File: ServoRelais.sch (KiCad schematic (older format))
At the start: 14 parts, among them J1 Conn_01x03_Female, J2 ISCP, J3 Conn_01x02_Female, J4 Conn_01x03_Female, U1 L78L05_SOT89, U2 PIC10F320-IP, U3 ASSR-1611

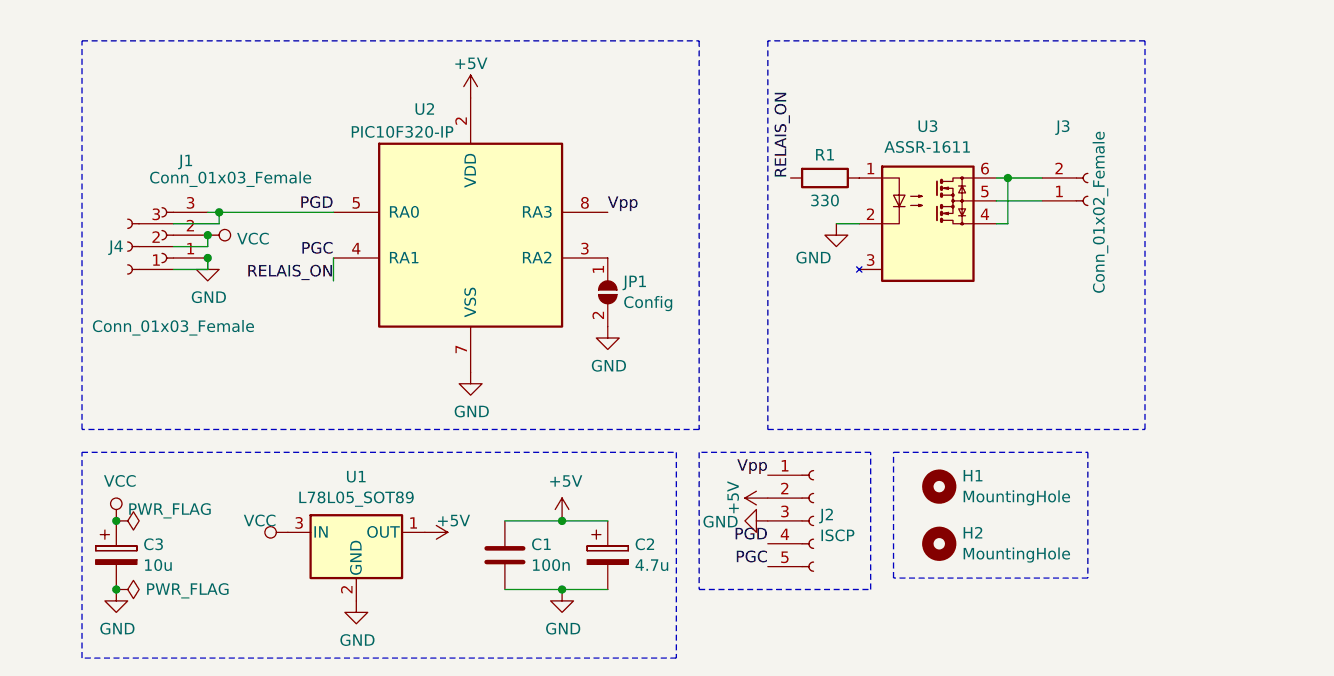
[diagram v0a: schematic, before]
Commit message: finish PCB, using ASSR-1611 as a 5A circuit breaker.
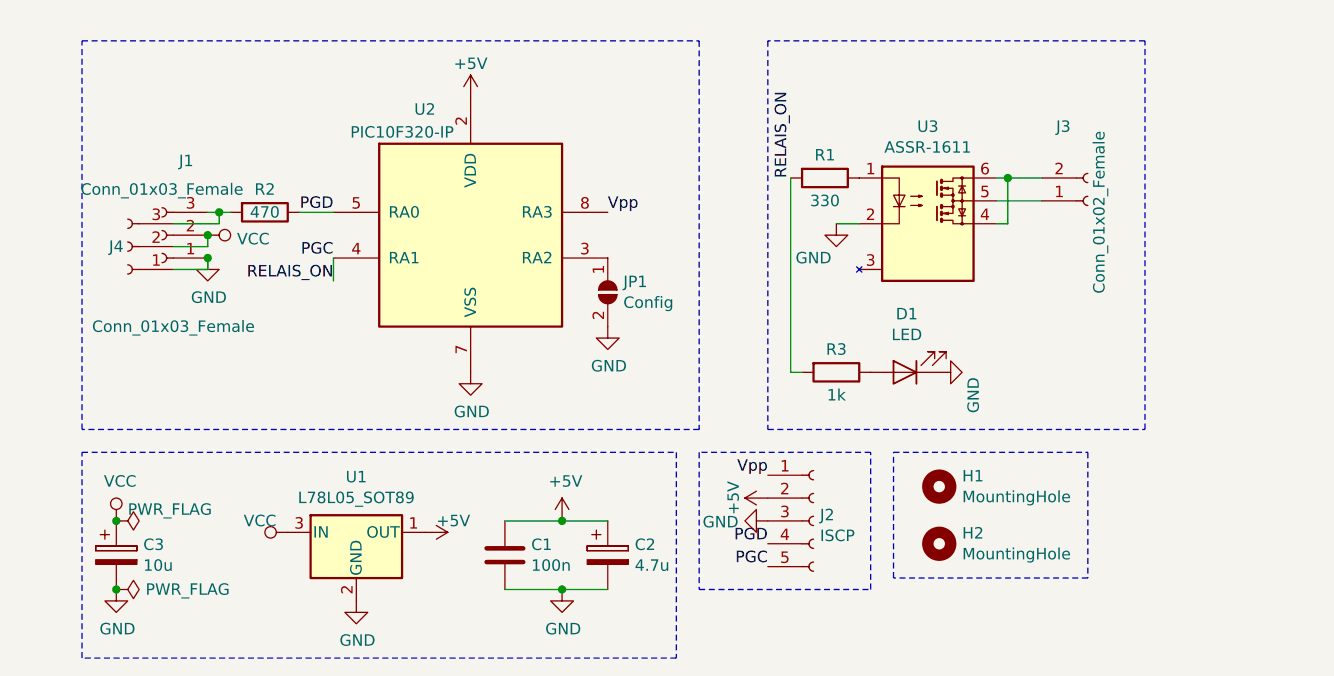
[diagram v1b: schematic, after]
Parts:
- added D1: LED, LEDs:LED_D3.0mm, symbol Device:LED
- added R2: 470, Resistors_ThroughHole:R_Axial_DIN0207_L6.3mm_D2.5mm_P7.62mm_Horizontal, symbol Device:R
- added R3: 1k, Resistors_ThroughHole:R_Axial_DIN0207_L6.3mm_D2.5mm_P7.62mm_Horizontal, symbol Device:R
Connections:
- net GND: now also D1.1 (K)
- net PGC: now also R3.2
- net PGD: now also R2.1; no longer J1.3 (Pin_3), J4.3 (Pin_3)
- new net: J1.3 (Pin_3), J4.3 (Pin_3), R2.2
- new net: D1.2 (A), R3.1
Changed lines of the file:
@@
 P 1050 1450
 F 0 "J1" H 944 1125 50  0000 C CNN
-F 1 "Conn_01x03_Female" H 750 1200 50  0000 C CNN
+F 1 "Conn_01x03_Female" H 1050 1250 50  0000 C CNN
 F 2 "Connectors_Molex:Molex_KK-6410-03_03x2.54mm_Straight" H 1050 1450 50  0001 C CNN
 F 3 "~" H 1050 1450 50  0001 C CNN
@@
 Wire Wire Line
 	1300 1400 1300 1350
-Connection ~ 1300 1350
-Wire Wire Line
-	1300 1350 1800 1350
 Wire Wire Line
 	1100 1500 1250 1500
@@
 $EndComp
 Connection ~ 850  2700
+$Comp
+L Device:R R2
+U 1 1 5FAE5A28
+P 1500 1350
+F 0 "R2" V 1400 1350 50  0000 C CNN
+F 1 "470" V 1500 1350 50  0000 C CNN
+F 2 "Resistors_ThroughHole:R_Axial_DIN0207_L6.3mm_D2.5mm_P7.62mm_Horizontal" V 1430 1350 50  0001 C CNN
+F 3 "~" H 1500 1350 50  0001 C CNN
+	1    1500 1350
+	0    1    1    0
+$EndComp
+Wire Wire Line
+	1300 1350 1350 1350
+Connection ~ 1300 1350
+Wire Wire Line
+	1650 1350 1800 1350
+$Comp
+L Device:R R3
+U 1 1 5FAE63BB
+P 4000 2050
+F 0 "R3" V 3900 2050 50  0000 C CNN
+F 1 "1k" V 4100 2050 50  0000 C CNN
+F 2 "Resistors_ThroughHole:R_Axial_DIN0207_L6.3mm_D2.5mm_P7.62mm_Horizontal" V 3930 2050 50  0001 C CNN
+F 3 "~" H 4000 2050 50  0001 C CNN
+	1    4000 2050
+	0    1    1    0
+$EndComp
+Wire Wire Line
+	3800 1200 3800 2050
+Wire Wire Line
+	3800 2050 3850 2050
+$Comp
+L Device:LED D1
+U 1 1 5FAE68AF
+P 4300 2050
+F 0 "D1" H 4292 1795 50  0000 C CNN
+F 1 "LED" H 4292 1886 50  0000 C CNN
+F 2 "LEDs:LED_D3.0mm" H 4300 2050 50  0001 C CNN
+F 3 "~" H 4300 2050 50  0001 C CNN
+	1    4300 2050
+	-1   0    0    1
+$EndComp
+$Comp
+L power:GND #PWR0116
+U 1 1 5FAE6927
+P 4450 2050
+F 0 "#PWR0116" H 4450 1800 50  0001 C CNN
+F 1 "GND" H 4350 1900 50  0000 C CNN
+F 2 "" H 4450 2050 50  0001 C CNN
+F 3 "" H 4450 2050 50  0001 C CNN
+	1    4450 2050
+	0    -1   -1   0
+$EndComp
 $EndSCHEMATC

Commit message: use a 3v->9V dc-dc converter. version 1.3
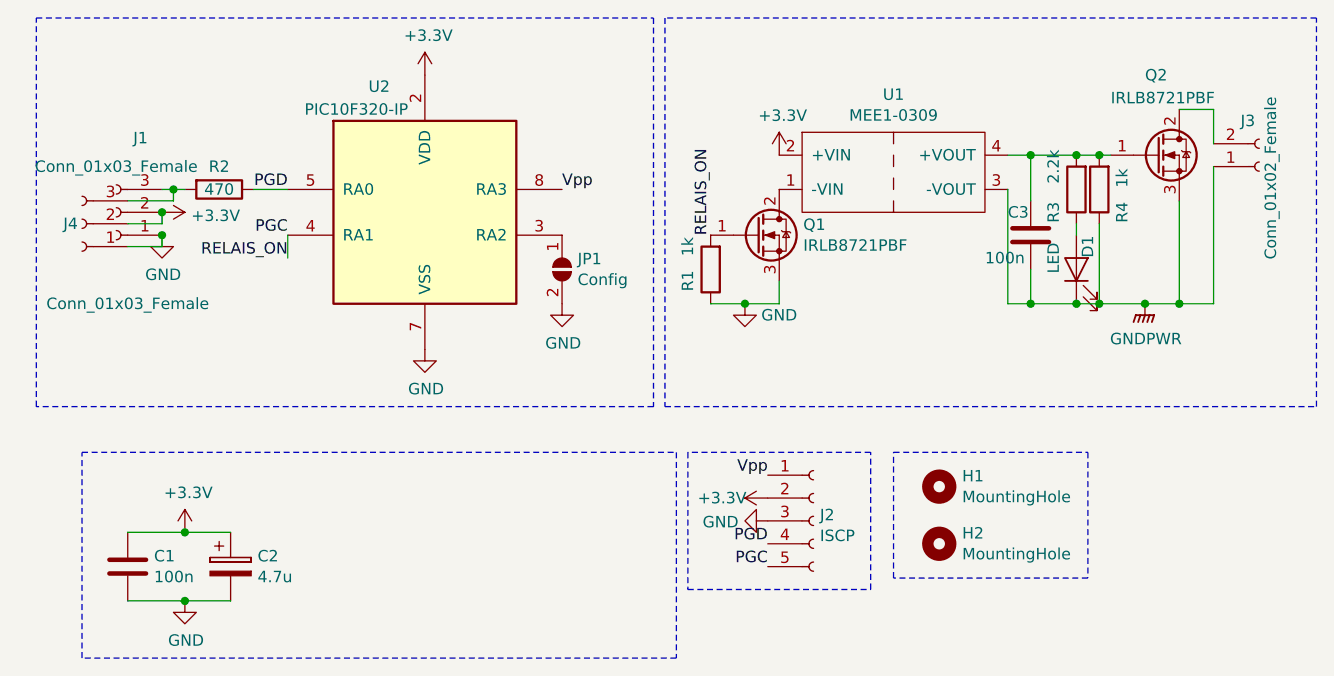
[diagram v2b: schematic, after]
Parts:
- removed C3: 10u, Capacitors_ThroughHole:CP_Radial_D4.0mm_P1.50mm, symbol Device:CP
- removed U1: L78L05_SOT89, TO_SOT_Packages_SMD:SOT-89-3_Handsoldering, symbol Regulator_Linear:L78L05_SOT89
- removed U3: ASSR-1611, Housings_DIP:DIP-6_W7.62mm_LongPads, symbol ServoRelais-rescue:ASSR-1611-ServoRelais
- added C3: 100n, Capacitors_ThroughHole:C_Rect_L4.6mm_W2.0mm_P2.50mm_MKS02_FKP02, symbol Device:C
- added Q1, Q2: IRLB8721PBF, TO_SOT_Packages_SMD:TO-252-2, symbol Transistor_FET:IRLB8721PBF
- added R4: 1k, Resistors_ThroughHole:R_Axial_DIN0207_L6.3mm_D2.5mm_P7.62mm_Horizontal, symbol Device:R
- added U1: MEE1-0309, Converters_DCDC_ACDC:DCDC-Conv_muRata_CRE1xxxxxxSC, symbol ServoRelais:MurataMEE1
- R1: value 330 -> 1k
- R3: value 1k -> 2.2k
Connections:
- net VCC is gone; now on net +3V3: J1.2 (Pin_2), J4.2 (Pin_2)
- net GND: now also R1.1, Q1.3 (S); no longer D1.1 (K)
- net PGC: now also Q1.1 (G); no longer R3.2
- net GNDPWR: now reaches J3.1 (Pin_1)
- net GNDPWR: now also D1.1 (K), C3.2, Q2.3 (S), R4.1, U1.3 (-VOUT)
- net at J3.2 (Pin_2): now also Q2.2 (D)
- net +5V renamed +3V3
- net +3V3: now also U1.2 (+VIN)
- new net: C3.1, Q2.1 (G), R3.2, R4.2, U1.4 (+VOUT)
- new net: Q1.2 (D), U1.1 (-VIN)
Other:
- moved on the sheet: C1, C2, D1, J1, J3, J4, JP1, R2, R3, U2

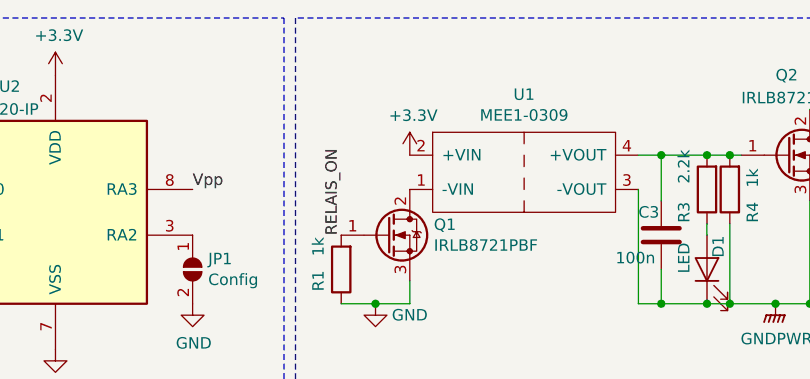
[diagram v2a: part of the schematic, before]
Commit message: PCB: add solder-switch to disable powering the DC-DC converter (else programming of the PIC fails because of power loss)
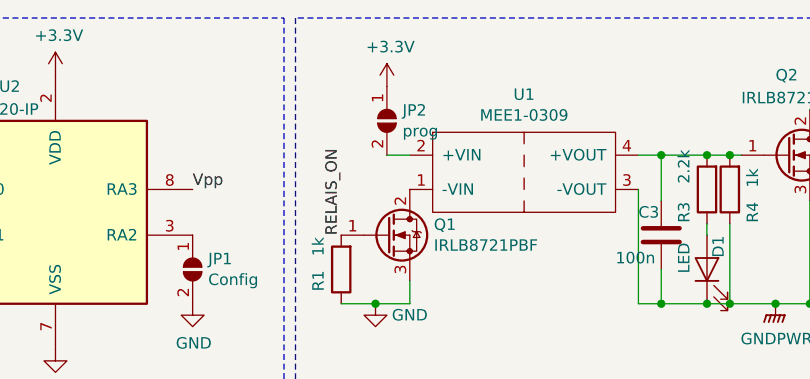
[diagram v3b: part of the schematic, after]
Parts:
- added JP2: prog, Connect:GS2, symbol Jumper:SolderJumper_2_Open
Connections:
- net +3V3: now also JP2.1 (A); no longer U1.2 (+VIN)
- new net: JP2.2 (B), U1.2 (+VIN)
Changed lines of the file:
@@
 L power:+3.3V #PWR04
 U 1 1 5FB40A3A
-P 3750 1100
-F 0 "#PWR04" H 3750 950 50  0001 C CNN
-F 1 "+3.3V" H 3765 1273 50  0000 C CNN
-F 2 "" H 3750 1100 50  0001 C CNN
-F 3 "" H 3750 1100 50  0001 C CNN
-	1    3750 1100
+P 3650 800
+F 0 "#PWR04" H 3650 650 50  0001 C CNN
+F 1 "+3.3V" H 3665 973 50  0000 C CNN
+F 2 "" H 3650 800 50  0001 C CNN
+F 3 "" H 3650 800 50  0001 C CNN
+	1    3650 800
 	1    0    0    -1
 $EndComp
@@
 Wire Wire Line
 	4850 1750 5050 1750
+$Comp
+L Jumper:SolderJumper_2_Open JP2
+U 1 1 5FB55293
+P 3650 950
+F 0 "JP2" V 3604 1018 50  0000 L CNN
+F 1 "prog" V 3695 1018 50  0000 L CNN
+F 2 "Connect:GS2" H 3650 950 50  0001 C CNN
+F 3 "~" H 3650 950 50  0001 C CNN
+	1    3650 950
+	0    1    1    0
+$EndComp
+Wire Wire Line
+	3650 1100 3750 1100
 $EndSCHEMATC

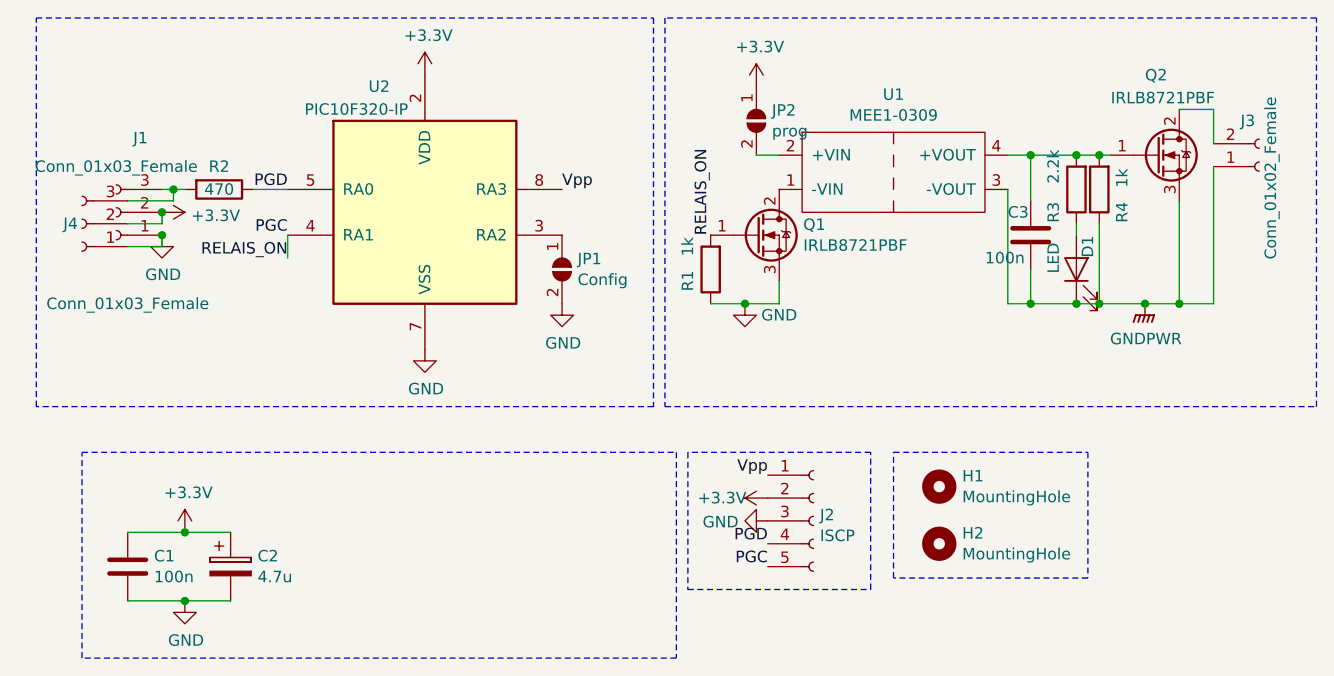
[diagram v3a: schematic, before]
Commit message: PCB 1.2: add 25Vmax->3V3 regulator
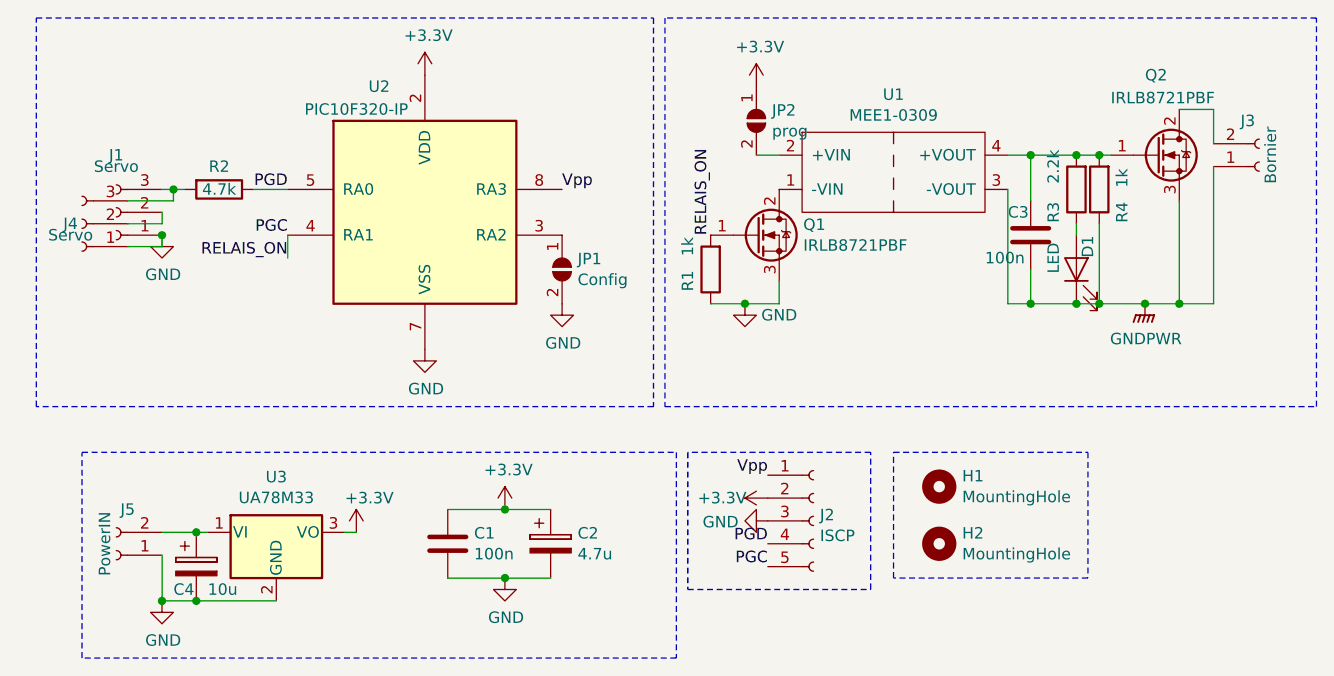
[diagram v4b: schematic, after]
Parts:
- added C4: 10u, Capacitors_ThroughHole:CP_Radial_D4.0mm_P1.50mm, symbol Device:CP
- added J5: PowerIN, Connectors_Molex:Molex_KK-6410-02_02x2.54mm_Straight, symbol Connector:Conn_01x02_Female
- added U3: UA78M33, TO_SOT_Packages_SMD:SOT-223-3_TabPin2, symbol Regulator_Linear:TC1262-33
- J1, J4: value Conn_01x03_Female -> Servo
- J3: value Conn_01x02_Female -> Bornier
- R2: value 470 -> 4.7k
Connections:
- net +3V3: now also U3.3 (VO); no longer J1.2 (Pin_2), J4.2 (Pin_2)
- net GND: now also C4.2, J5.1 (Pin_1), U3.2 (GND)
- new net: J1.2 (Pin_2), J4.2 (Pin_2)
- new net: C4.1, J5.2 (Pin_2), U3.1 (VI)
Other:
- moved on the sheet: C1, C2
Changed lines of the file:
@@
 Sheet 1 1
 Title "ServoRelais"
-Date "2020-11-12"
-Rev "1"
+Date "2020-12-22"
+Rev "1.2"
 Comp "metalu.net"
 Comment1 ""
@@
 U 1 1 5FAAD2A2
 P 850 1350
-F 0 "J1" H 744 1025 50  0000 C CNN
-F 1 "Conn_01x03_Female" H 850 1150 50  0000 C CNN
+F 0 "J1" H 850 1100 50  0000 C CNN
+F 1 "Servo" H 850 1150 50  0000 C CNN
 F 2 "Connectors_Molex:Molex_KK-6410-03_03x2.54mm_Straight" H 850 1350 50  0001 C CNN
 F 3 "~" H 850 1350 50  0001 C CNN
@@
 P 5850 1150
 F 0 "J3" H 5800 950 50  0000 C CNN
-F 1 "Conn_01x02_Female" V 5900 1200 50  0000 C CNN
+F 1 "Bornier" V 5900 1100 50  0000 C CNN
 F 2 "Terminal_Blocks:TerminalBlock_bornier-2_P5.08mm" H 5850 1150 50  0001 C CNN
 F 3 "~" H 5850 1150 50  0001 C CNN
@@
 L Device:C C1
 U 1 1 5FAAF3D2
-P 900 2900
-F 0 "C1" H 1015 2946 50  0000 L CNN
-F 1 "100n" H 1015 2855 50  0000 L CNN
-F 2 "Capacitors_ThroughHole:C_Rect_L4.6mm_W2.0mm_P2.50mm_MKS02_FKP02" H 938 2750 50  0001 C CNN
-F 3 "~" H 900 2900 50  0001 C CNN
-	1    900  2900
+P 2300 2800
+F 0 "C1" H 2415 2846 50  0000 L CNN
+F 1 "100n" H 2415 2755 50  0000 L CNN
+F 2 "Capacitors_ThroughHole:C_Rect_L4.6mm_W2.0mm_P2.50mm_MKS02_FKP02" H 2338 2650 50  0001 C CNN
+F 3 "~" H 2300 2800 50  0001 C CNN
+	1    2300 2800
 	1    0    0    -1
 $EndComp
@@
 L Device:CP C2
 U 1 1 5FAAF4A0
-P 1350 2900
-F 0 "C2" H 1468 2946 50  0000 L CNN
-F 1 "4.7u" H 1468 2855 50  0000 L CNN
-F 2 "Capacitors_ThroughHole:CP_Radial_D4.0mm_P1.50mm" H 1388 2750 50  0001 C CNN
-F 3 "~" H 1350 2900 50  0001 C CNN
-	1    1350 2900
-	1    0    0    -1
-$EndComp
-Wire Wire Line
-	900  3050 1150 3050
+P 2750 2800
+F 0 "C2" H 2868 2846 50  0000 L CNN
+F 1 "4.7u" H 2868 2755 50  0000 L CNN
+F 2 "Capacitors_ThroughHole:CP_Radial_D4.0mm_P1.50mm" H 2788 2650 50  0001 C CNN
+F 3 "~" H 2750 2800 50  0001 C CNN
+	1    2750 2800
+	1    0    0    -1
+$EndComp
+Wire Wire Line
+	2300 2950 2550 2950
 $Comp
 L power:GND #PWR0112
 U 1 1 5FAAF6AE
-P 1150 3050
-F 0 "#PWR0112" H 1150 2800 50  0001 C CNN
-F 1 "GND" H 1155 2877 50  0000 C CNN
-F 2 "" H 1150 3050 50  0001 C CNN
-F 3 "" H 1150 3050 50  0001 C CNN
-	1    1150 3050
-	1    0    0    -1
-$EndComp
-Connection ~ 1150 3050
-Wire Wire Line
-	1150 3050 1350 3050
+P 2550 2950
+F 0 "#PWR0112" H 2550 2700 50  0001 C CNN
+F 1 "GND" H 2555 2777 50  0000 C CNN
+F 2 "" H 2550 2950 50  0001 C CNN
+F 3 "" H 2550 2950 50  0001 C CNN
+	1    2550 2950
+	1    0    0    -1
+$EndComp
+Connection ~ 2550 2950
+Wire Wire Line
+	2550 2950 2750 2950
 $Comp
 L MCU_Microchip_PIC10:PIC10F320-IP U2
@@
 P 700 1400
 F 0 "J4" H 750 1400 50  0000 C CNN
-F 1 "Conn_01x03_Female" H 500 1750 50  0000 C CNN
+F 1 "Servo" H 750 1450 50  0000 C CNN
 F 2 "Connectors_Molex:Molex_KK-6410-03_03x2.54mm_Straight" H 700 1400 50  0001 C CNN
 F 3 "~" H 700 1400 50  0001 C CNN
@@
 P 1300 1250
 F 0 "R2" V 1200 1250 50  0000 C CNN
-F 1 "470" V 1300 1250 50  0000 C CNN
+F 1 "4.7k" V 1300 1250 50  0000 C CNN
 F 2 "Resistors_ThroughHole:R_Axial_DIN0207_L6.3mm_D2.5mm_P7.62mm_Horizontal" V 1230 1250 50  0001 C CNN
 F 3 "~" H 1300 1250 50  0001 C CNN
@@
 L power:+3.3V #PWR02
 U 1 1 5FB3FC34
-P 1150 2750
-F 0 "#PWR02" H 1150 2600 50  0001 C CNN
-F 1 "+3.3V" H 1165 2923 50  0000 C CNN
-F 2 "" H 1150 2750 50  0001 C CNN
-F 3 "" H 1150 2750 50  0001 C CNN
-	1    1150 2750
-	1    0    0    -1
-$EndComp
-Wire Wire Line
-	900  2750 1150 2750
-Connection ~ 1150 2750
-Wire Wire Line
-	1150 2750 1350 2750
+P 2550 2650
+F 0 "#PWR02" H 2550 2500 50  0001 C CNN
+F 1 "+3.3V" H 2565 2823 50  0000 C CNN
+F 2 "" H 2550 2650 50  0001 C CNN
+F 3 "" H 2550 2650 50  0001 C CNN
+	1    2550 2650
+	1    0    0    -1
+$EndComp
+Wire Wire Line
+	2300 2650 2550 2650
+Connection ~ 2550 2650
+Wire Wire Line
+	2550 2650 2750 2650
 $Comp
 L power:+3.3V #PWR01
 U 1 1 5FB4090A
-P 1050 1350
-F 0 "#PWR01" H 1050 1200 50  0001 C CNN
-F 1 "+3.3V" V 1065 1478 50  0000 L CNN
-F 2 "" H 1050 1350 50  0001 C CNN
-F 3 "" H 1050 1350 50  0001 C CNN
-	1    1050 1350
-	0    1    1    0
-$EndComp
-Connection ~ 1050 1350
+P 1900 2750
+F 0 "#PWR01" H 1900 2600 50  0001 C CNN
+F 1 "+3.3V" H 1850 2900 50  0000 L CNN
+F 2 "" H 1900 2750 50  0001 C CNN
+F 3 "" H 1900 2750 50  0001 C CNN
+	1    1900 2750
+	1    0    0    -1
+$EndComp
 $Comp
 L power:+3.3V #PWR03
@@
 Wire Wire Line
 	3650 1100 3750 1100
+$Comp
+L Regulator_Linear:TC1262-33 U3
+U 1 1 5FE1DAA9
+P 1550 2750
+F 0 "U3" H 1550 2992 50  0000 C CNN
+F 1 "UA78M33" H 1550 2901 50  0000 C CNN
+F 2 "TO_SOT_Packages_SMD:SOT-223-3_TabPin2" H 1550 2975 50  0001 C CIN
+F 3 "http://ww1.microchip.com/downloads/en/DeviceDoc/21373C.pdf" H 1550 2450 50  0001 C CNN
+	1    1550 2750
+	1    0    0    -1
+$EndComp
+$Comp
+L Device:CP C4
+U 1 1 5FE1DC64
+P 1200 2900
+F 0 "C4" H 1100 2800 50  0000 L CNN
+F 1 "10u" H 1250 2800 50  0000 L CNN
+F 2 "Capacitors_ThroughHole:CP_Radial_D4.0mm_P1.50mm" H 1238 2750 50  0001 C CNN
+F 3 "~" H 1200 2900 50  0001 C CNN
+	1    1200 2900
+	1    0    0    -1
+$EndComp
+$Comp
+L Connector:Conn_01x02_Female J5
+U 1 1 5FE1EC47
+P 850 2850
+F 0 "J5" H 800 2650 50  0000 C CNN
+F 1 "PowerIN" V 900 2800 50  0000 C CNN
+F 2 "Connectors_Molex:Molex_KK-6410-02_02x2.54mm_Straight" H 850 2850 50  0001 C CNN
+F 3 "~" H 850 2850 50  0001 C CNN
+	1    850  2850
+	-1   0    0    1
+$EndComp
+$Comp
+L power:GND #PWR05
+U 1 1 5FE203ED
+P 1050 3050
+F 0 "#PWR05" H 1050 2800 50  0001 C CNN
+F 1 "GND" H 1055 2877 50  0000 C CNN
+F 2 "" H 1050 3050 50  0001 C CNN
+F 3 "" H 1050 3050 50  0001 C CNN
+	1    1050 3050
+	1    0    0    -1
+$EndComp
+Wire Wire Line
+	1050 2850 1050 3050
+Wire Wire Line
+	1050 3050 1200 3050
+Connection ~ 1050 3050
+Wire Wire Line
+	1200 3050 1550 3050
+Connection ~ 1200 3050
+Wire Wire Line
+	1900 2750 1850 2750
+Wire Wire Line
+	1250 2750 1200 2750
+Wire Wire Line
+	1200 2750 1050 2750
+Connection ~ 1200 2750
 $EndSCHEMATC
